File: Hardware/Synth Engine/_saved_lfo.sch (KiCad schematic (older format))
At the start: 26 parts, among them J5 Conn_01x02, J6 Conn_01x03, U4 TL074, U5 TL074

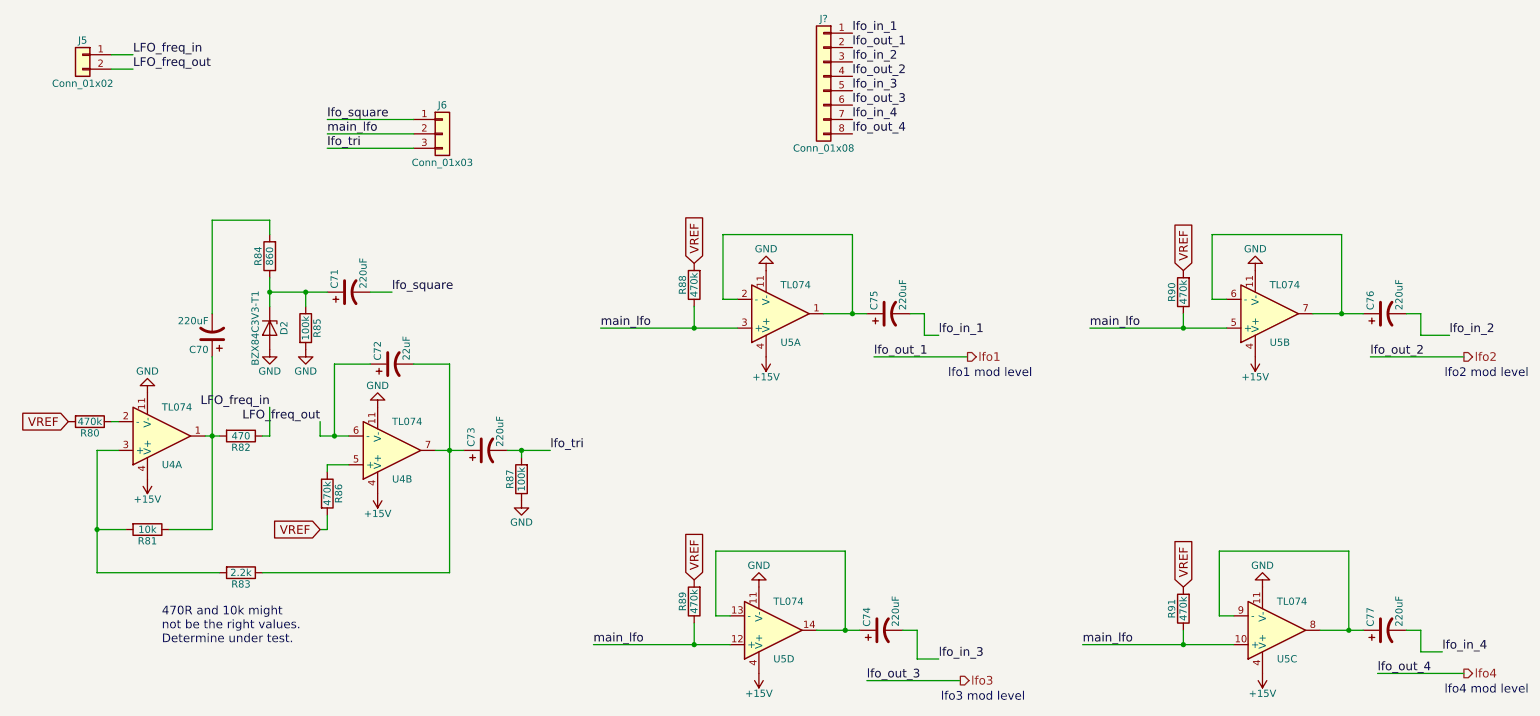
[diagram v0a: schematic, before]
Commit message: route traces to bypass caps on MCU. control board and connectors are WIP.
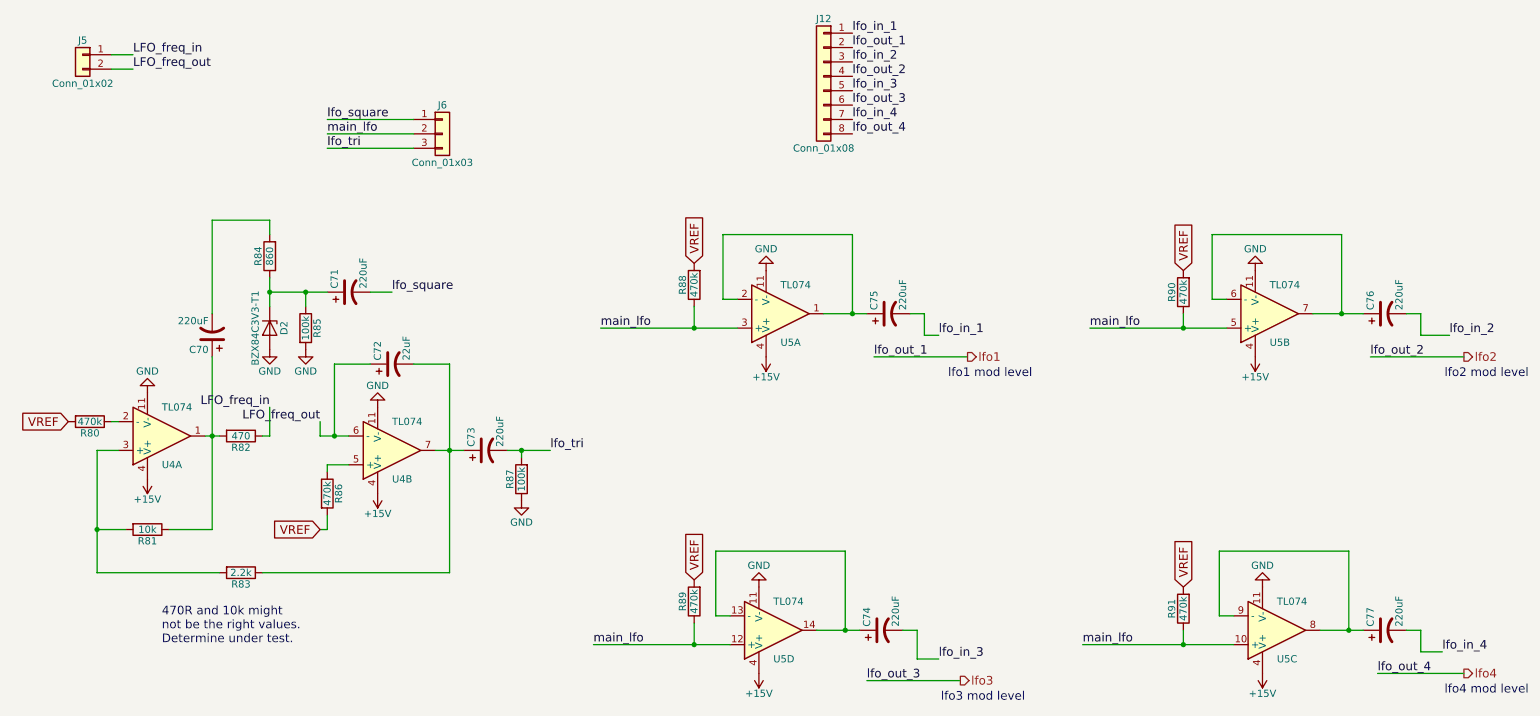
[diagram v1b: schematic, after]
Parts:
- J12: renamed from J?; footprint (none) -> Pin_Headers:Pin_Header_Straight_1x08_Pitch2.54mm
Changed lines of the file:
@@
 main_lfo
 $Comp
-L GND #PWR099
+L GND #PWR095
 U 1 1 5C541D9A
 P 5750 2450
-F 0 "#PWR099" H 5750 2200 50  0001 C CNN
+F 0 "#PWR095" H 5750 2200 50  0001 C CNN
 F 1 "GND" H 5750 2300 50  0000 C CNN
 F 2 "" H 5750 2450 50  0001 C CNN
@@
 $EndComp
 $Comp
-L +15V #PWR0100
+L +15V #PWR096
 U 1 1 5C541DA0
 P 5750 3050
-F 0 "#PWR0100" H 5750 2900 50  0001 C CNN
+F 0 "#PWR096" H 5750 2900 50  0001 C CNN
 F 1 "+15V" H 5750 3190 50  0000 C CNN
 F 2 "" H 5750 3050 50  0001 C CNN
@@
 main_lfo
 $Comp
-L GND #PWR0101
+L GND #PWR097
 U 1 1 5C542158
 P 9150 2450
-F 0 "#PWR0101" H 9150 2200 50  0001 C CNN
+F 0 "#PWR097" H 9150 2200 50  0001 C CNN
 F 1 "GND" H 9150 2300 50  0000 C CNN
 F 2 "" H 9150 2450 50  0001 C CNN
@@
 $EndComp
 $Comp
-L +15V #PWR0102
+L +15V #PWR098
 U 1 1 5C54215E
 P 9150 3050
-F 0 "#PWR0102" H 9150 2900 50  0001 C CNN
+F 0 "#PWR098" H 9150 2900 50  0001 C CNN
 F 1 "+15V" H 9150 3190 50  0000 C CNN
 F 2 "" H 9150 3050 50  0001 C CNN
@@
 main_lfo
 $Comp
-L GND #PWR0103
+L GND #PWR099
 U 1 1 5C5423E6
 P 5700 4650
-F 0 "#PWR0103" H 5700 4400 50  0001 C CNN
+F 0 "#PWR099" H 5700 4400 50  0001 C CNN
 F 1 "GND" H 5700 4500 50  0000 C CNN
 F 2 "" H 5700 4650 50  0001 C CNN
@@
 $EndComp
 $Comp
-L +15V #PWR0104
+L +15V #PWR0100
 U 1 1 5C5423EC
 P 5700 5250
-F 0 "#PWR0104" H 5700 5100 50  0001 C CNN
+F 0 "#PWR0100" H 5700 5100 50  0001 C CNN
 F 1 "+15V" H 5700 5390 50  0000 C CNN
 F 2 "" H 5700 5250 50  0001 C CNN
@@
 main_lfo
 $Comp
-L GND #PWR0105
+L GND #PWR0101
 U 1 1 5C5426E0
 P 9200 4650
-F 0 "#PWR0105" H 9200 4400 50  0001 C CNN
+F 0 "#PWR0101" H 9200 4400 50  0001 C CNN
 F 1 "GND" H 9200 4500 50  0000 C CNN
 F 2 "" H 9200 4650 50  0001 C CNN
@@
 $EndComp
 $Comp
-L +15V #PWR0106
+L +15V #PWR0102
 U 1 1 5C5426E6
 P 9200 5250
-F 0 "#PWR0106" H 9200 5100 50  0001 C CNN
+F 0 "#PWR0102" H 9200 5100 50  0001 C CNN
 F 1 "+15V" H 9200 5390 50  0000 C CNN
 F 2 "" H 9200 5250 50  0001 C CNN
@@
 	10200 4950 10300 4950
 Wire Wire Line
-	9600 4950 9800 4950
-Wire Wire Line
-	9800 4950 9900 4950
+	9600 4950 9900 4950
 Wire Wire Line
 	10200 2750 10300 2750
 Wire Wire Line
-	9550 2750 9750 2750
-Wire Wire Line
-	9750 2750 9900 2750
+	9550 2750 9900 2750
 Wire Wire Line
 	6700 4950 6800 4950
 Wire Wire Line
-	6100 4950 6300 4950
-Wire Wire Line
-	6300 4950 6400 4950
+	6100 4950 6400 4950
 Wire Wire Line
 	6750 2750 6850 2750
 Wire Wire Line
-	6150 2750 6350 2750
-Wire Wire Line
-	6350 2750 6450 2750
+	6150 2750 6450 2750
 Connection ~ 8650 5050
 Wire Wire Line
@@
 	9800 4950 9800 4400
 Wire Wire Line
-	7950 5050 8650 5050
-Wire Wire Line
-	8650 5050 9000 5050
+	7950 5050 9000 5050
 Connection ~ 6300 4950
 Wire Wire Line
@@
 	6300 4950 6300 4400
 Wire Wire Line
-	4550 5050 5250 5050
-Wire Wire Line
-	5250 5050 5500 5050
+	4550 5050 5500 5050
 Connection ~ 9750 2750
 Wire Wire Line
@@
 	9750 2750 9750 2200
 Wire Wire Line
-	8000 2850 8650 2850
-Wire Wire Line
-	8650 2850 8950 2850
+	8000 2850 8950 2850
 Connection ~ 6350 2750
 Wire Wire Line
@@
 	6350 2750 6350 2200
 Wire Wire Line
-	4600 2850 5250 2850
-Wire Wire Line
-	5250 2850 5550 2850
+	4600 2850 5550 2850
 Wire Wire Line
 	6500 3050 7150 3050
@@
 Connection ~ 2300 2600
 Wire Wire Line
-	2300 2600 2550 2600
-Wire Wire Line
-	2550 2600 2700 2600
+	2300 2600 2700 2600
 Wire Wire Line
 	2300 2100 2300 2200
@@
 	1900 2100 2300 2100
 Wire Wire Line
-	2300 2500 2300 2600
-Wire Wire Line
-	2300 2600 2300 2700
+	2300 2500 2300 2700
 Wire Wire Line
 	2700 3800 2850 3800
 Wire Wire Line
-	2650 3600 2750 3600
-Wire Wire Line
-	2750 3600 2850 3600
-Wire Wire Line
-	3450 3700 3550 3700
-Wire Wire Line
-	3550 3700 3650 3700
+	2650 3600 2850 3600
+Wire Wire Line
+	3450 3700 3650 3700
 Wire Wire Line
 	1250 3700 1100 3700
@@
 Connection ~ 4050 3700
 Wire Wire Line
-	3950 3700 4050 3700
-Wire Wire Line
-	4050 3700 4250 3700
+	3950 3700 4250 3700
 Wire Wire Line
 	4050 3750 4050 3700
@@
 	3550 4550 2250 4550
 Wire Wire Line
-	1100 3700 1100 4250
-Wire Wire Line
-	1100 4250 1100 4550
+	1100 3700 1100 4550
 Wire Wire Line
 	1300 4250 1100 4250
@@
 	1900 4250 1600 4250
 Wire Wire Line
-	1900 3050 1900 3600
-Wire Wire Line
-	1900 3600 1900 4250
+	1900 3050 1900 4250
 Wire Wire Line
 	2700 3850 2700 3800
@@
 	3550 3100 3300 3100
 Wire Wire Line
-	3550 3100 3550 3700
-Wire Wire Line
-	3550 3700 3550 4550
-Wire Wire Line
-	1850 3600 1900 3600
-Wire Wire Line
-	1900 3600 1950 3600
+	3550 3100 3550 4550
+Wire Wire Line
+	1850 3600 1950 3600
 Wire Wire Line
 	2250 3600 2300 3600
@@
 lfo_out_4
 $Comp
-L Conn_01x08 J?
+L Conn_01x08 J12
 U 1 1 5C638F36
 P 6150 1100
-F 0 "J?" H 6150 1500 50  0000 C CNN
+F 0 "J12" H 6150 1500 50  0000 C CNN
 F 1 "Conn_01x08" H 6150 600 50  0000 C CNN
-F 2 "" H 6150 1100 50  0001 C CNN
+F 2 "Pin_Headers:Pin_Header_Straight_1x08_Pitch2.54mm" H 6150 1100 50  0001 C CNN
 F 3 "" H 6150 1100 50  0001 C CNN
 	1    6150 1100
